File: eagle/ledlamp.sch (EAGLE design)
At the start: 22 parts

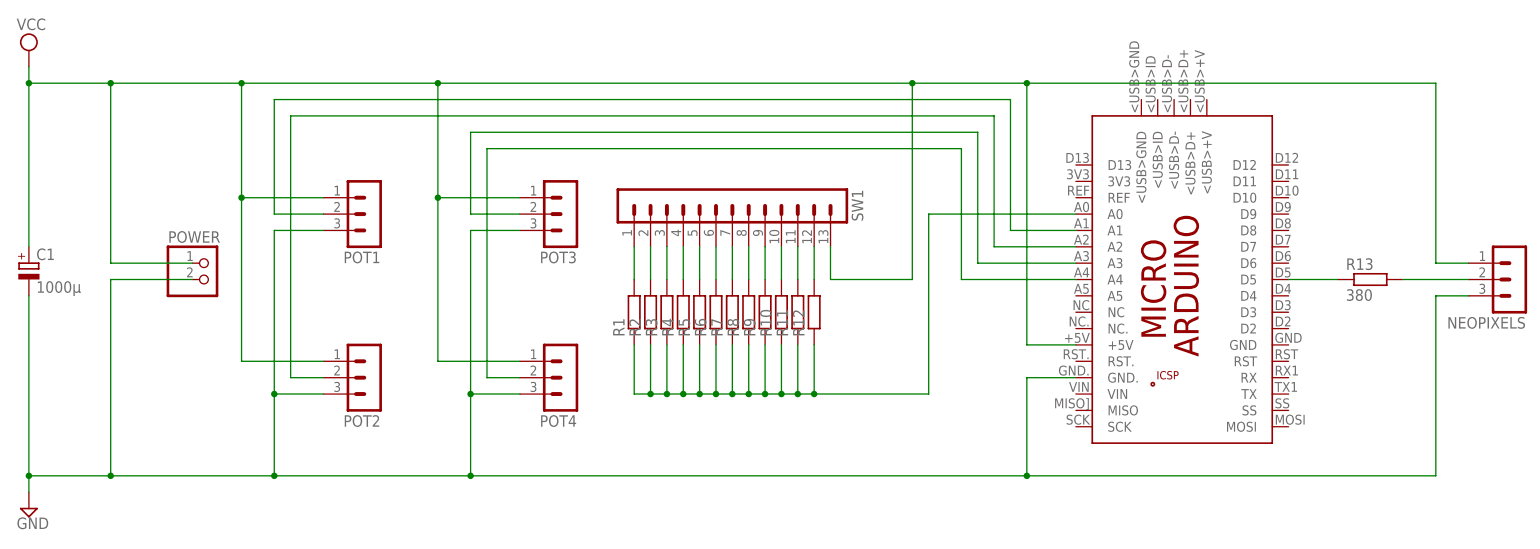
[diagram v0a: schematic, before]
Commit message: Add pull-down resistor as voltage divider for A0
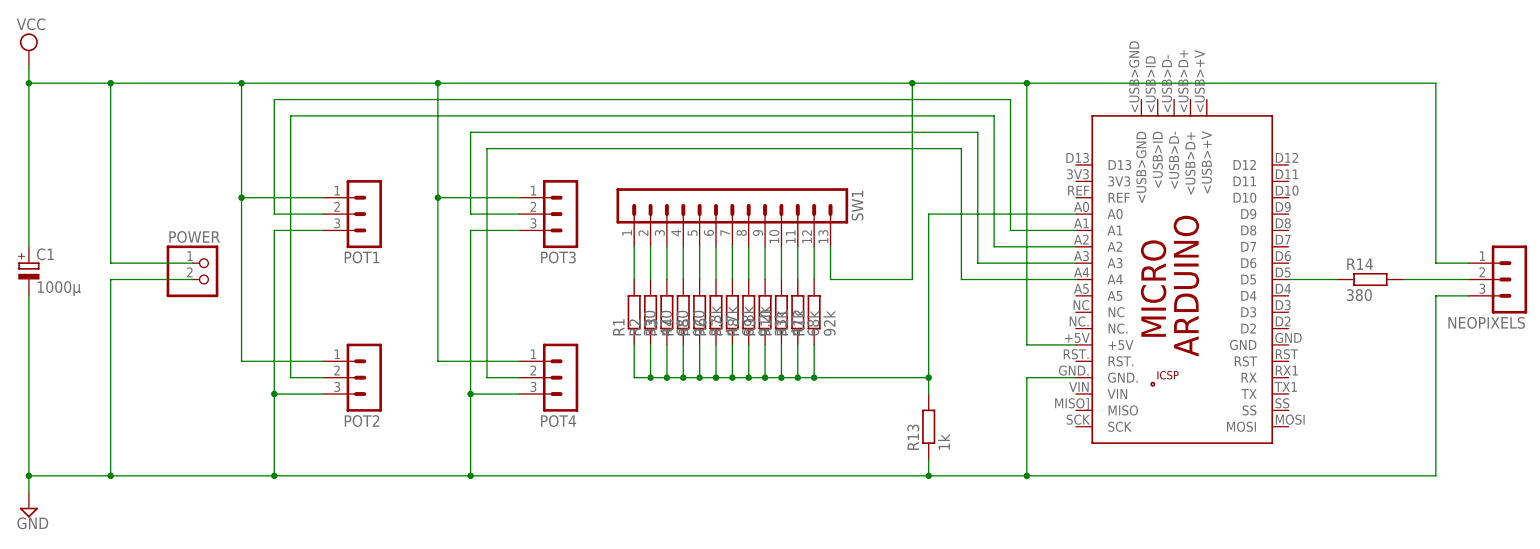
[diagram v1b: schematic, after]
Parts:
- added R14: 380, rcl:R-EU_0207/10
- R1: value (none) -> 330
- R10: value (none) -> 47k
- R11: value (none) -> 68k
- R12: value (none) -> 92k
- R13: value 380 -> 1k
- R2: value (none) -> 470
- R3: value (none) -> 680
- R4: value (none) -> 920
- R5: value (none) -> 3.3k
- R6: value (none) -> 4.7k
- R7: value (none) -> 6.8k
- R8: value (none) -> 9.2k
- R9: value (none) -> 33k
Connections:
- net GND: now also R13.1
- net N$14: now also R13.2
- net N$22: now also R14.1; no longer R13.1
- net N$23: now also R14.2; no longer R13.2
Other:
- moved on the sheet: R13
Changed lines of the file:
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@@
 <part name="POT4" library="con-lstb" deviceset="MA03-1" device=""/>
 <part name="SW1" library="con-lstb" deviceset="MA13-1" device=""/>
-<part name="R1" library="rcl" deviceset="R-EU_" device="0207/10"/>
-<part name="R2" library="rcl" deviceset="R-EU_" device="0207/10"/>
-<part name="R3" library="rcl" deviceset="R-EU_" device="0207/10"/>
-<part name="R4" library="rcl" deviceset="R-EU_" device="0207/10"/>
-<part name="R5" library="rcl" deviceset="R-EU_" device="0207/10"/>
-<part name="R6" library="rcl" deviceset="R-EU_" device="0207/10"/>
-<part name="R7" library="rcl" deviceset="R-EU_" device="0207/10"/>
-<part name="R8" library="rcl" deviceset="R-EU_" device="0207/10"/>
-<part name="R9" library="rcl" deviceset="R-EU_" device="0207/10"/>
-<part name="R10" library="rcl" deviceset="R-EU_" device="0207/10"/>
-<part name="R11" library="rcl" deviceset="R-EU_" device="0207/10"/>
-<part name="R12" library="rcl" deviceset="R-EU_" device="0207/10"/>
+<part name="R1" library="rcl" deviceset="R-EU_" device="0207/10" value="330"/>
+<part name="R2" library="rcl" deviceset="R-EU_" device="0207/10" value="470"/>
+<part name="R3" library="rcl" deviceset="R-EU_" device="0207/10" value="680"/>
+<part name="R4" library="rcl" deviceset="R-EU_" device="0207/10" value="920"/>
+<part name="R5" library="rcl" deviceset="R-EU_" device="0207/10" value="3.3k"/>
+<part name="R6" library="rcl" deviceset="R-EU_" device="0207/10" value="4.7k"/>
+<part name="R7" library="rcl" deviceset="R-EU_" device="0207/10" value="6.8k"/>
+<part name="R8" library="rcl" deviceset="R-EU_" device="0207/10" value="9.2k"/>
+<part name="R9" library="rcl" deviceset="R-EU_" device="0207/10" value="33k"/>
+<part name="R10" library="rcl" deviceset="R-EU_" device="0207/10" value="47k"/>
+<part name="R11" library="rcl" deviceset="R-EU_" device="0207/10" value="68k"/>
+<part name="R12" library="rcl" deviceset="R-EU_" device="0207/10" value="92k"/>
 <part name="PCB1" library="E14_Arduino_revB" deviceset="ARDUINO_MICRO" device=""/>
-<part name="R13" library="rcl" deviceset="R-EU_" device="0207/10" value="380"/>
+<part name="R14" library="rcl" deviceset="R-EU_" device="0207/10" value="380"/>
 <part name="NEOPIXELS" library="con-lstb" deviceset="MA03-1" device=""/>
 <part name="POWER" library="pinhead" deviceset="PINHD-1X2" device=""/>
+<part name="R13" library="rcl" deviceset="R-EU_" device="0207/10" value="1k"/>
 </parts>
 <sheets>
@@
 <instance part="R12" gate="G$1" x="132.08" y="33.02" rot="R90"/>
 <instance part="PCB1" gate="G$1" x="190.5" y="38.1" rot="R270"/>
-<instance part="R13" gate="G$1" x="218.44" y="38.1"/>
+<instance part="R14" gate="G$1" x="218.44" y="38.1"/>
 <instance part="NEOPIXELS" gate="G$1" x="241.3" y="38.1" rot="R180"/>
 <instance part="POWER" gate="G$1" x="38.1" y="38.1"/>
+<instance part="R13" gate="G$1" x="149.86" y="15.24" rot="R90"/>
 </instances>
 <busses>
@@
 <wire x1="172.72" y1="22.86" x2="165.1" y2="22.86" width="0.1524" layer="91"/>
 <wire x1="165.1" y1="22.86" x2="165.1" y2="7.62" width="0.1524" layer="91"/>
-<wire x1="165.1" y1="7.62" x2="78.74" y2="7.62" width="0.1524" layer="91"/>
+<wire x1="165.1" y1="7.62" x2="149.86" y2="7.62" width="0.1524" layer="91"/>
 <junction x="78.74" y="7.62"/>
 <pinref part="NEOPIXELS" gate="G$1" pin="3"/>
+<wire x1="149.86" y1="7.62" x2="78.74" y2="7.62" width="0.1524" layer="91"/>
 <wire x1="233.68" y1="35.56" x2="228.6" y2="35.56" width="0.1524" layer="91"/>
 <wire x1="228.6" y1="35.56" x2="228.6" y2="7.62" width="0.1524" layer="91"/>
@@
 <wire x1="22.86" y1="38.1" x2="22.86" y2="7.62" width="0.1524" layer="91"/>
 <junction x="22.86" y="7.62"/>
+<pinref part="R13" gate="G$1" pin="1"/>
+<wire x1="149.86" y1="10.16" x2="149.86" y2="7.62" width="0.1524" layer="91"/>
+<junction x="149.86" y="7.62"/>
 </segment>
 </net>
@@
 <segment>
 <pinref part="R1" gate="G$1" pin="1"/>
-<wire x1="104.14" y1="27.94" x2="104.14" y2="20.32" width="0.1524" layer="91"/>
-<wire x1="104.14" y1="20.32" x2="106.68" y2="20.32" width="0.1524" layer="91"/>
+<wire x1="104.14" y1="27.94" x2="104.14" y2="22.86" width="0.1524" layer="91"/>
+<wire x1="104.14" y1="22.86" x2="106.68" y2="22.86" width="0.1524" layer="91"/>
 <pinref part="R2" gate="G$1" pin="1"/>
-<wire x1="106.68" y1="20.32" x2="109.22" y2="20.32" width="0.1524" layer="91"/>
-<wire x1="109.22" y1="20.32" x2="111.76" y2="20.32" width="0.1524" layer="91"/>
-<wire x1="111.76" y1="20.32" x2="114.3" y2="20.32" width="0.1524" layer="91"/>
-<wire x1="114.3" y1="20.32" x2="116.84" y2="20.32" width="0.1524" layer="91"/>
-<wire x1="116.84" y1="20.32" x2="119.38" y2="20.32" width="0.1524" layer="91"/>
-<wire x1="119.38" y1="20.32" x2="121.92" y2="20.32" width="0.1524" layer="91"/>
-<wire x1="121.92" y1="20.32" x2="124.46" y2="20.32" width="0.1524" layer="91"/>
-<wire x1="124.46" y1="20.32" x2="127" y2="20.32" width="0.1524" layer="91"/>
-<wire x1="127" y1="20.32" x2="129.54" y2="20.32" width="0.1524" layer="91"/>
-<wire x1="129.54" y1="20.32" x2="132.08" y2="20.32" width="0.1524" layer="91"/>
-<wire x1="132.08" y1="20.32" x2="149.86" y2="20.32" width="0.1524" layer="91"/>
-<wire x1="106.68" y1="27.94" x2="106.68" y2="20.32" width="0.1524" layer="91"/>
+<wire x1="106.68" y1="22.86" x2="109.22" y2="22.86" width="0.1524" layer="91"/>
+<wire x1="109.22" y1="22.86" x2="111.76" y2="22.86" width="0.1524" layer="91"/>
+<wire x1="111.76" y1="22.86" x2="114.3" y2="22.86" width="0.1524" layer="91"/>
+<wire x1="114.3" y1="22.86" x2="116.84" y2="22.86" width="0.1524" layer="91"/>
+<wire x1="116.84" y1="22.86" x2="119.38" y2="22.86" width="0.1524" layer="91"/>
+<wire x1="119.38" y1="22.86" x2="121.92" y2="22.86" width="0.1524" layer="91"/>
+<wire x1="121.92" y1="22.86" x2="124.46" y2="22.86" width="0.1524" layer="91"/>
+<wire x1="124.46" y1="22.86" x2="127" y2="22.86" width="0.1524" layer="91"/>
+<wire x1="127" y1="22.86" x2="129.54" y2="22.86" width="0.1524" layer="91"/>
+<wire x1="129.54" y1="22.86" x2="132.08" y2="22.86" width="0.1524" layer="91"/>
+<wire x1="132.08" y1="22.86" x2="149.86" y2="22.86" width="0.1524" layer="91"/>
+<wire x1="106.68" y1="27.94" x2="106.68" y2="22.86" width="0.1524" layer="91"/>
 <pinref part="R3" gate="G$1" pin="1"/>
-<wire x1="109.22" y1="20.32" x2="109.22" y2="27.94" width="0.1524" layer="91"/>
+<wire x1="109.22" y1="22.86" x2="109.22" y2="27.94" width="0.1524" layer="91"/>
 <pinref part="R4" gate="G$1" pin="1"/>
-<wire x1="111.76" y1="27.94" x2="111.76" y2="20.32" width="0.1524" layer="91"/>
+<wire x1="111.76" y1="27.94" x2="111.76" y2="22.86" width="0.1524" layer="91"/>
 <pinref part="R5" gate="G$1" pin="1"/>
-<wire x1="114.3" y1="20.32" x2="114.3" y2="27.94" width="0.1524" layer="91"/>
+<wire x1="114.3" y1="22.86" x2="114.3" y2="27.94" width="0.1524" layer="91"/>
 <pinref part="R6" gate="G$1" pin="1"/>
-<wire x1="116.84" y1="27.94" x2="116.84" y2="20.32" width="0.1524" layer="91"/>
+<wire x1="116.84" y1="27.94" x2="116.84" y2="22.86" width="0.1524" layer="91"/>
 <pinref part="R7" gate="G$1" pin="1"/>
-<wire x1="119.38" y1="20.32" x2="119.38" y2="27.94" width="0.1524" layer="91"/>
+<wire x1="119.38" y1="22.86" x2="119.38" y2="27.94" width="0.1524" layer="91"/>
 <pinref part="R8" gate="G$1" pin="1"/>
-<wire x1="121.92" y1="27.94" x2="121.92" y2="20.32" width="0.1524" layer="91"/>
+<wire x1="121.92" y1="27.94" x2="121.92" y2="22.86" width="0.1524" layer="91"/>
 <pinref part="R9" gate="G$1" pin="1"/>
-<wire x1="124.46" y1="20.32" x2="124.46" y2="27.94" width="0.1524" layer="91"/>
+<wire x1="124.46" y1="22.86" x2="124.46" y2="27.94" width="0.1524" layer="91"/>
 <pinref part="R10" gate="G$1" pin="1"/>
-<wire x1="127" y1="27.94" x2="127" y2="20.32" width="0.1524" layer="91"/>
+<wire x1="127" y1="27.94" x2="127" y2="22.86" width="0.1524" layer="91"/>
 <pinref part="R11" gate="G$1" pin="1"/>
-<wire x1="129.54" y1="20.32" x2="129.54" y2="27.94" width="0.1524" layer="91"/>
+<wire x1="129.54" y1="22.86" x2="129.54" y2="27.94" width="0.1524" layer="91"/>
 <pinref part="R12" gate="G$1" pin="1"/>
-<wire x1="132.08" y1="27.94" x2="132.08" y2="20.32" width="0.1524" layer="91"/>
-<junction x="106.68" y="20.32"/>
-<junction x="109.22" y="20.32"/>
-<junction x="111.76" y="20.32"/>
-<junction x="114.3" y="20.32"/>
-<junction x="116.84" y="20.32"/>
-<junction x="119.38" y="20.32"/>
-<junction x="121.92" y="20.32"/>
-<junction x="124.46" y="20.32"/>
-<junction x="127" y="20.32"/>
-<junction x="129.54" y="20.32"/>
-<junction x="132.08" y="20.32"/>
+<wire x1="132.08" y1="27.94" x2="132.08" y2="22.86" width="0.1524" layer="91"/>
+<junction x="106.68" y="22.86"/>
+<junction x="109.22" y="22.86"/>
+<junction x="111.76" y="22.86"/>
+<junction x="114.3" y="22.86"/>
+<junction x="116.84" y="22.86"/>
+<junction x="119.38" y="22.86"/>
+<junction x="121.92" y="22.86"/>
+<junction x="124.46" y="22.86"/>
+<junction x="127" y="22.86"/>
+<junction x="129.54" y="22.86"/>
+<junction x="132.08" y="22.86"/>
 <pinref part="PCB1" gate="G$1" pin="A0"/>
 <wire x1="172.72" y1="48.26" x2="149.86" y2="48.26" width="0.1524" layer="91"/>
-<wire x1="149.86" y1="48.26" x2="149.86" y2="20.32" width="0.1524" layer="91"/>
+<wire x1="149.86" y1="48.26" x2="149.86" y2="22.86" width="0.1524" layer="91"/>
+<pinref part="R13" gate="G$1" pin="2"/>
+<wire x1="149.86" y1="22.86" x2="149.86" y2="20.32" width="0.1524" layer="91"/>
+<junction x="149.86" y="22.86"/>
 </segment>
 </net>
@@
 <pinref part="PCB1" gate="G$1" pin="D5"/>
 <wire x1="205.74" y1="38.1" x2="213.36" y2="38.1" width="0.1524" layer="91"/>
-<pinref part="R13" gate="G$1" pin="1"/>
+<pinref part="R14" gate="G$1" pin="1"/>
 </segment>
 </net>
 <net name="N$23" class="0">
 <segment>
-<pinref part="R13" gate="G$1" pin="2"/>
+<pinref part="R14" gate="G$1" pin="2"/>
 <pinref part="NEOPIXELS" gate="G$1" pin="2"/>
 <wire x1="223.52" y1="38.1" x2="233.68" y2="38.1" width="0.1524" layer="91"/>
